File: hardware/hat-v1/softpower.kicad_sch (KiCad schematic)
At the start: 14 parts, among them J6 PANEL BTN, Q10 BSS138, SW1 on-board PWR, U9 LTC2955ITS8-2#TRPBF

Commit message: HAT v1 schematic: apply adversarial review (power + digital/security/DFM)
AUTO-ON above buck EN window, BENCH no longer blocks power-off, OVP moved
to 19.2 V with input damper, Tier A parts DNP for JLC, debug links
removable for production, antenna short limited, stock footprints where
available, cap ratings/DC-bias fixes, CONSOLE_TX/RX naming.

Co-Authored-By: Claude Opus 5.5 <noreply@anthropic.com>
Claude-Session: https://claude.ai/code/session_01MLRuxTEmuMV82xcNLE62jW
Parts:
- JP3: now left out of the parts list
- R31: value 681k 1% -> 787k 1%; Note (none) -> AUTO-ON 7.10 V typ / 6.74 V min: above the 5 V buck EN max 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
- R32: Note ON 0.8 V -> auto-on at 6.25 V -> (none)
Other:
- note added: "NOTES U9: -2 = active-low EN-bar (900k to VIN when off); KILL blanking 304-720 ms R30: gate = 0.53 x VSYS when off (<=9.7 V) C41: long-press force-off ~5.3 s JP3: close: power-on automatically when input appears (mast relay / C0 / T0) R31: AUTO-ON 7.10 V typ / 6.74 V min: above the 5 V buck EN max 6.55 V (review P1) R33: KILL high as soon as the Pi 3.3 V is up Q10: GPIO27 high (gpio-poweroff) -> 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"
- note removed: "NOTES U9: -2 = active-low EN-bar (900k to VIN when off); KILL blanking 304-720 ms R30: gate = 0.53 x VSYS when off (<=9.7 V) C41: long-press force-off ~5.3 s JP3: close: power-on automatically when input appears (mast relay / C0 / T0) R32: ON 0.8 V -> auto-on at 6.25 V R33: KILL high as soon as the Pi 3.3 V is up Q10: GPIO27 high (gpio-poweroff) -> power off R34: reboot: GPIO27 default pull-down 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"
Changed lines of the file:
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@@
   (global_label "GND" (shape passive) (at 167.64 26.67 0) (fields_autoplaced) (effects (font (size 1.27 1.27)) (justify left))
     (property "Intersheetrefs" "${INTERSHEET_REFS}" (at 167.64 26.67 0) (effects (font (size 1.27 1.27)) hide)))
-  (symbol (lib_id "batman:SJ") (at 194.31 26.67 0) (unit 1) (in_bom yes) (on_board yes) (dnp no)
+  (symbol (lib_id "batman:SJ") (at 194.31 26.67 0) (unit 1) (in_bom no) (on_board yes) (dnp no)
     (property "Reference" "JP3" (at 194.31 24.13 0) (effects (font (size 1.27 1.27)) (justify bottom)))
     (property "Value" "AUTO-ON (open)" (at 194.31 29.21 0) (effects (font (size 1.27 1.27)) (justify top)))
@@
   (symbol (lib_id "batman:R") (at 224.79 26.67 0) (unit 1) (in_bom yes) (on_board yes) (dnp no)
     (property "Reference" "R31" (at 224.79 24.13 0) (effects (font (size 1.27 1.27)) (justify bottom)))
-    (property "Value" "681k 1%" (at 224.79 29.21 0) (effects (font (size 1.27 1.27)) (justify top)))
+    (property "Value" "787k 1%" (at 224.79 29.21 0) (effects (font (size 1.27 1.27)) (justify top)))
     (property "Footprint" "Resistor_SMD:R_0402_1005Metric" (at 224.79 26.67 0) (effects (font (size 1.27 1.27)) hide))
     (property "Datasheet" "" (at 224.79 26.67 0) (effects (font (size 1.27 1.27)) hide))
@@
     (property "Tier" "C" (at 224.79 26.67 0) (effects (font (size 1.27 1.27)) hide))
     (property "LCSC" "" (at 224.79 26.67 0) (effects (font (size 1.27 1.27)) hide))
-    (property "Note" "" (at 224.79 26.67 0) (effects (font (size 1.27 1.27)) hide))
+    (property "Note" "AUTO-ON 7.10 V typ / 6.74 V min: above the 5 V buck EN max 6.55 V (review P1)" (at 224.79 26.67 0) (effects (font (size 1.27 1.27)) hide))
     (pin "1")
     (pin "2")
@@
     (property "Tier" "C" (at 256.54 26.67 0) (effects (font (size 1.27 1.27)) hide))
     (property "LCSC" "" (at 256.54 26.67 0) (effects (font (size 1.27 1.27)) hide))
-    (property "Note" "ON 0.8 V -> auto-on at 6.25 V" (at 256.54 26.67 0) (effects (font (size 1.27 1.27)) hide))
+    (property "Note" "" (at 256.54 26.67 0) (effects (font (size 1.27 1.27)) hide))
     (pin "1")
     (pin "2")
@@
   (global_label "GND" (shape passive) (at 40.64 72.39 0) (fields_autoplaced) (effects (font (size 1.27 1.27)) (justify left))
     (property "Intersheetrefs" "${INTERSHEET_REFS}" (at 40.64 72.39 0) (effects (font (size 1.27 1.27)) hide)))
-  (text "NOTES\nU9: -2 = active-low EN-bar (900k to VIN when off); KILL blanking 304-720 ms\nR30: gate = 0.53 x VSYS when off (<=9.7 V)\nC41: long-press force-off ~5.3 s\nJP3: close: power-on automatically when input appears (mast relay / C0 / T0)\nR32: ON 0.8 V -> auto-on at 6.25 V\nR33: KILL high as soon as the Pi 3.3 V is up\nQ10: GPIO27 high (gpio-poweroff) -> power off\nR34: reboot: GPIO27 default pull-down keeps power on\nSW1: low-profile side button for the bench\nJ6: to the IP67 panel push-button\nD4: ESD for the panel button wire" (at 15 82.94 0) (effects (font (size 1.27 1.27)) (justify left top)))
+  (text "NOTES\nU9: -2 = active-low EN-bar (900k to VIN when off); KILL blanking 304-720 ms\nR30: gate = 0.53 x VSYS when off (<=9.7 V)\nC41: long-press force-off ~5.3 s\nJP3: close: power-on automatically when input appears (mast relay / C0 / T0)\nR31: AUTO-ON 7.10 V typ / 6.74 V min: above the 5 V buck EN max 6.55 V (review P1)\nR33: KILL high as soon as the Pi 3.3 V is up\nQ10: GPIO27 high (gpio-poweroff) -> power off\nR34: reboot: GPIO27 default pull-down keeps power on\nSW1: low-profile side button for the bench\nJ6: to the IP67 panel push-button\nD4: ESD for the panel button wire" (at 15 82.94 0) (effects (font (size 1.27 1.27)) (justify left top)))
 )

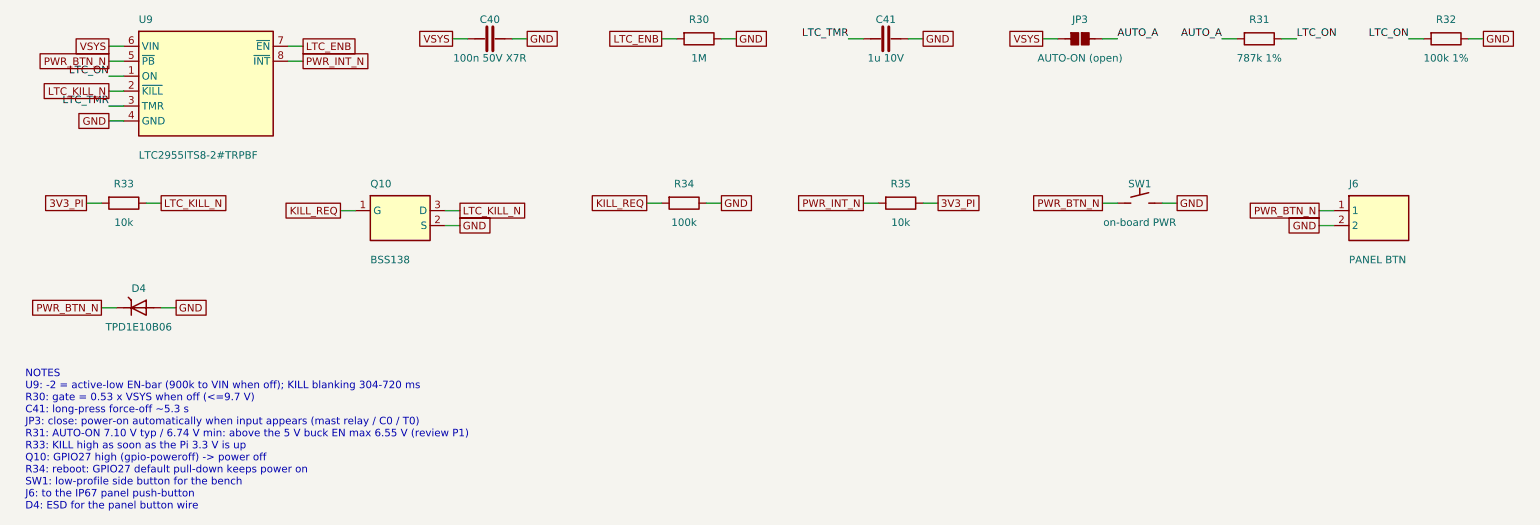
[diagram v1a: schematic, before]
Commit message: HAT v1: hand placement of the power path (5V buck at the header, battery bottom-left), routing pipeline
layout.py: anchors for ~45 power/IC parts, proximity placement for the rest,
net classes, In1 GND plane (Specctra power layer), DSN export, Freerouting,
SES import, power-track widening, GND pours, DRC. SW1 and C7 removed
(user decision / space). Wi-Fi keep-out reduced to an L shape so header
pins 1-4 stay routable.

Co-Authored-By: Claude Opus 5.5 <noreply@anthropic.com>
Claude-Session: https://claude.ai/code/session_01MLRuxTEmuMV82xcNLE62jW
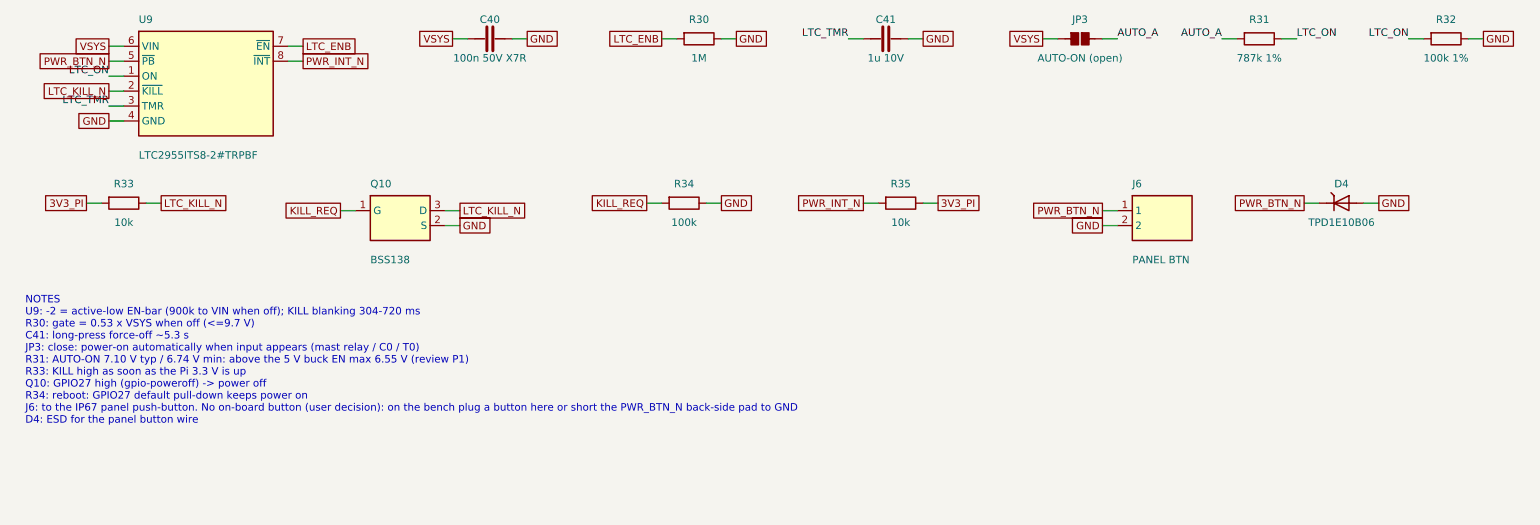
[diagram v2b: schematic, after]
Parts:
- removed SW1: on-board PWR, Button_Switch_SMD:SW_SPST_EVQP7A, symbol batman:SW_PUSH
- J6: Note to the IP67 panel push-button -> to the IP67 panel push-button. No on-board button (user dec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
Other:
- moved on the sheet: D4, J6
